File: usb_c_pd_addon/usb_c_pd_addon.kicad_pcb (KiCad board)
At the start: 2 copper layers, 40 x 10 mm, 17 parts, among them J1 USB-C_Female, J3 Conn_01x05, J4 Conn_01x03, J5 Conn_01x01, U1 FUSB302MPX, U2 TPS2592xx

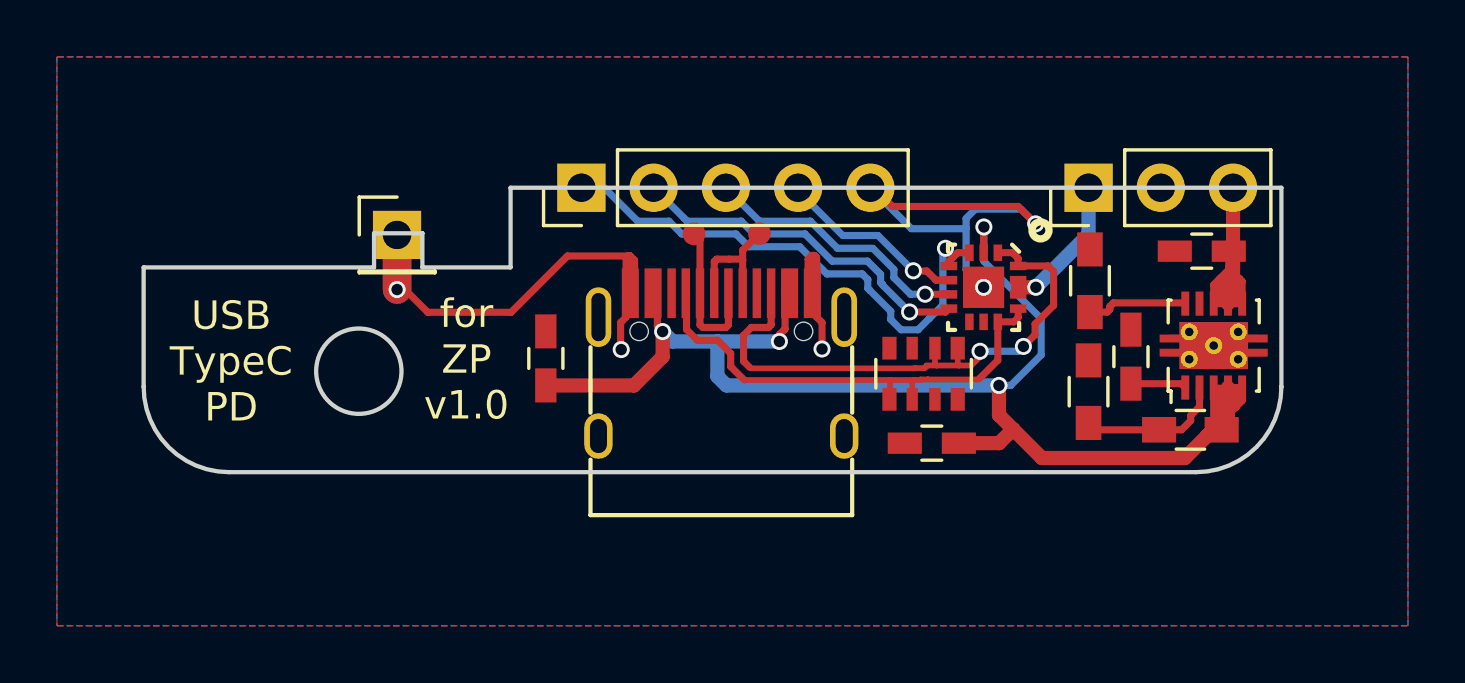
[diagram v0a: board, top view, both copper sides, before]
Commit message: USB Type-C mod - v1.0
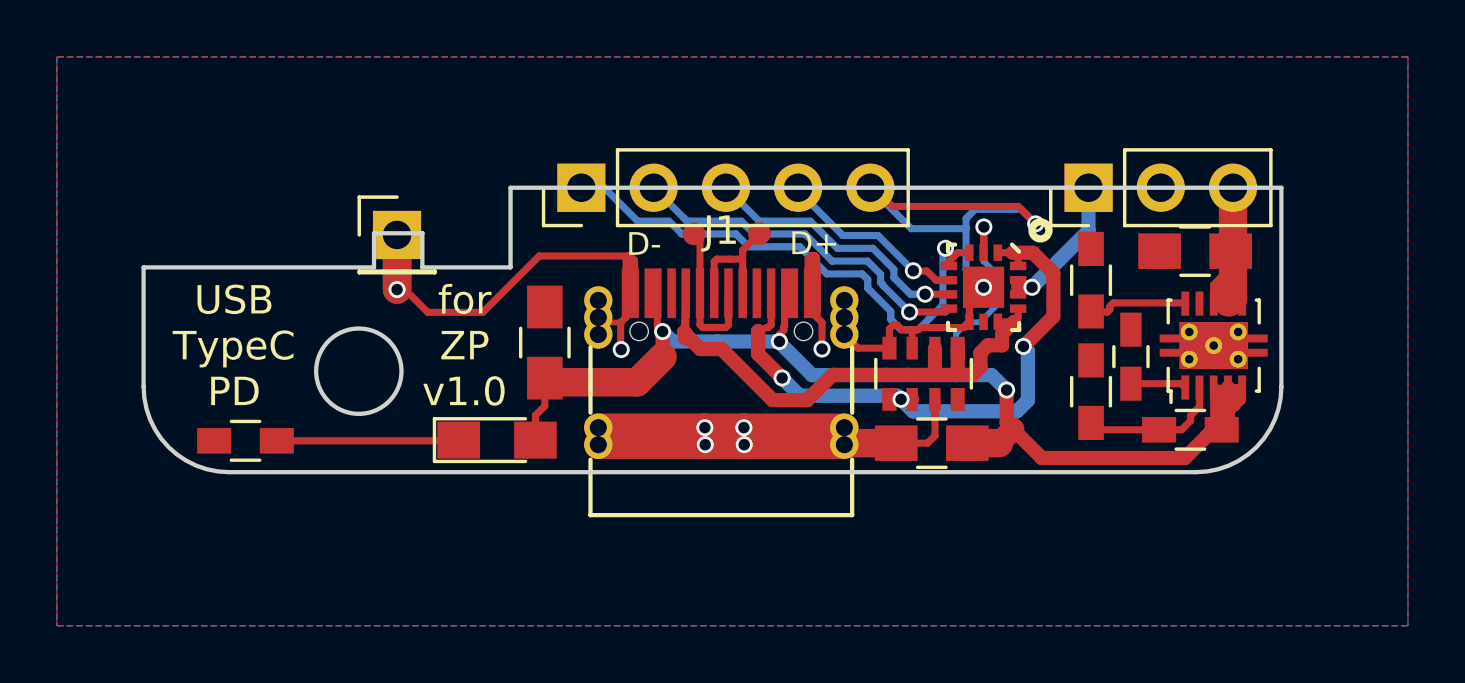
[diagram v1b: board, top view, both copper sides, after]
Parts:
- added D1: LED, LEDs:LED_0805_HandSoldering, F.Cu at (95.5, 111.0)
- added R4: 10K, Resistors_SMD:R_0603_HandSoldering, F.Cu at (86.6, 111.0)
- C2, C3, C4: footprint Capacitors_SMD:C_0603_HandSoldering -> Capacitors_SMD:C_0805_HandSoldering
- moved C2 0.56 mm to (97.2, 107.5)
- moved C4 0.23 mm to (120.0, 104.3)
- moved R2 0.09 mm to (116.4, 109.3)
- turned RN1 to 270 degrees
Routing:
- net GND: track 46.4 -> 87.5 mm, vias 5 -> 9
- net Net-(D1-Pad1): track 0.00 -> 6.40 mm
- net Net-(C4-Pad1): track 10.7 -> 14.8 mm
- net CC1: track 17.4 -> 20.6 mm
- net VBUS: track 52.0 -> 50.3 mm
- net CC2: track 20.3 -> 21.7 mm, vias 2 -> 3
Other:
- board text added: "D+"
- board text added: "D-"
